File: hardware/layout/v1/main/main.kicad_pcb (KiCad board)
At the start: 4 copper layers, 32 x 52 mm, 53 parts, among them J1 12-32V + RS485, J2 Crown board, J3 Probe board, J4 PMSA003I PM, J5 Power board, Q1 AO3400A, SW1 SERVICE, U2 LM66100, U3 XIAO ESP32C6, U4 ADS1115IDGSR, U5 LSM6DS3TR-C, U6 AS3935-BQFT, U7 SP3485EN-L/TR, U8 SN74LVC2G04DBVR

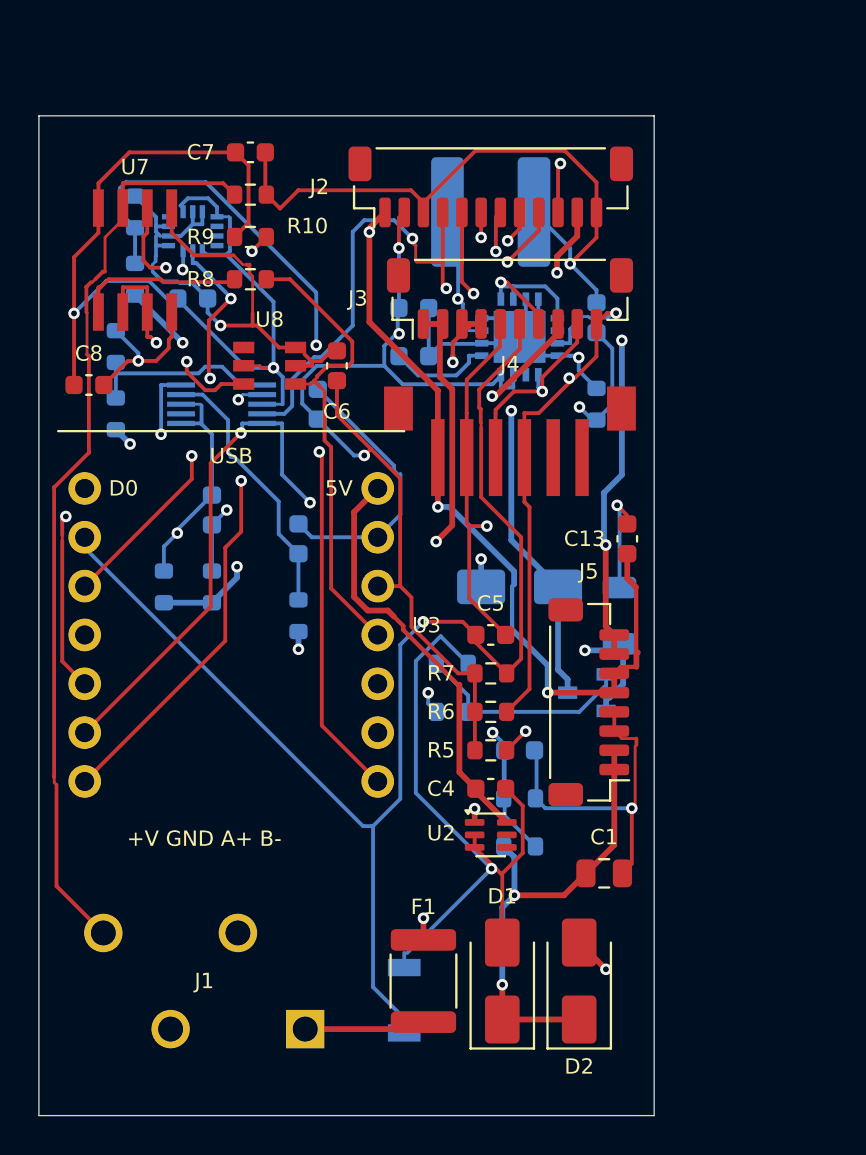
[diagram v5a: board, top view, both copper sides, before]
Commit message: Update documentation for 60V power system, STM32 crown board, 12V heaters, and expanded enclosure design
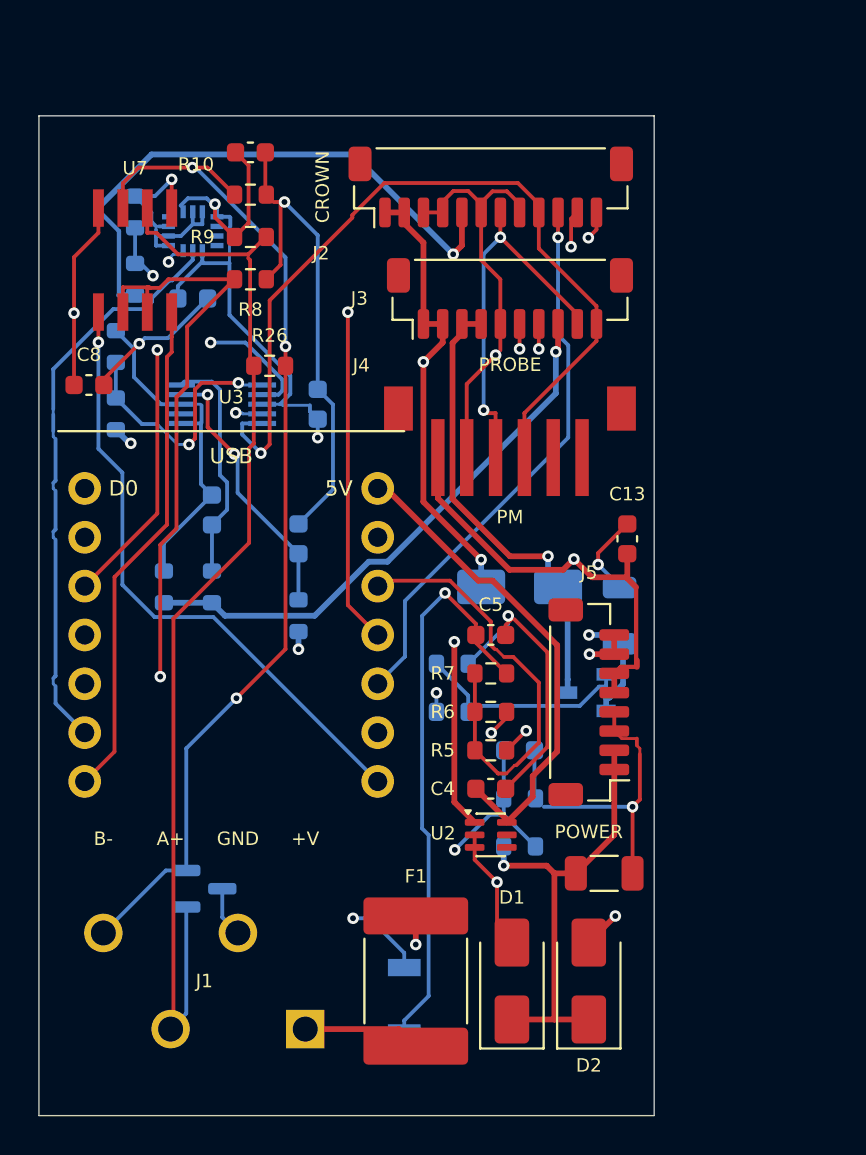
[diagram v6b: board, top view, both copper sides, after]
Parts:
- removed C10: 1u 50V, Capacitor_SMD:C_0603_1608Metric
- removed C11, C6: 100n 50V, Capacitor_SMD:C_0603_1608Metric
- removed C12: 470p C0G 50V, Capacitor_SMD:C_0603_1608Metric
- removed L2: 220uH, Inductor_SMD:L_Sunlord_SWPA6045S
- removed R11: 10k, Resistor_SMD:R_0603_1608Metric
- removed U6: AS3935-BQFT, gateway_fp:ScioSense_AS3935_QFN-16
- removed U8: SN74LVC2G04DBVR, gateway_fp:TI_SN74LVC2G04_SOT-23-6
- added D4: PSM712, Package_TO_SOT_SMD:SOT-23, B.Cu at (8.60, -11.8)
- added R26: 120R, Resistor_SMD:R_0603_1608Metric, F.Cu at (12.0, -39.0)
- C1: value 10u 50V -> 2u2 100V; footprint Capacitor_SMD:C_0805_2012Metric -> Capacitor_SMD:C_1206_3216Metric
- D1: value SMAJ33A -> SMAJ36A
- F1: footprint Fuse:Fuse_1812_4532Metric -> Fuse:Fuse_2920_7451Metric
- R10, R9: value 4k7 -> 390R
- R20: value 10k -> 30k
- R5, R6: value 4k7 -> 2k2
- R8: value 1k -> 10k
- moved D1 0.50 mm to (24.6, -7.00)
- moved D2 0.50 mm to (28.6, -7.00)
- moved F1 0.40 mm to (19.6, -7.00)
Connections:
- D3 pad 1: +5V_HEAT -> +12V_HEAT
- J2 pad 1: +5V -> +12V_HEAT
- J2 pad 10: RAIN_ADC -> CROWN_IRQ
- J2 pad 11: +5V_HEAT -> CROWN_NRST
- J2 pad 12: GND -> CROWN_BOOT0
- J2 pad 2: +3V3 -> +12V_HEAT
- J2 pad 4: I2C_SDA -> GND
- J2 pad 5: I2C_SCL -> +5V
- J2 pad 6: US_SEL_A -> GND
- J2 pad 7: US_SEL_B -> I2C_SDA
- J2 pad 8: US_TX -> GND
- J2 pad 9: US_RX -> I2C_SCL
- J3 pad 1: +5V_HEAT -> +12V_HEAT
- J3 pad 2: +5V_HEAT -> +12V_HEAT
- J5 pad 7: +5V_HEAT -> +12V_HEAT
- J5 pad 8: +5V_HEAT -> +12V_HEAT
- R20 pad 1: +5V_HEAT -> +12V_HEAT
- R8 pad 1: RS485_RO -> RS485_DE
- R8 pad 2: RS485_IO -> GND
- U3 pad 10: US_RX -> CROWN_IRQ
- U3 pad 11: RS485_IO -> CROWN_NRST
- U3 pad 3: RAIN_ADC -> CROWN_BOOT0
- U3 pad 7: US_SEL_A -> RS485_TX
- U3 pad 8: US_SEL_B -> RS485_RX
- U3 pad 9: US_TX -> RS485_DE
- U7 pad 1: RS485_RO -> RS485_RX
- U7 pad 4: GND -> RS485_TX
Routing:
- net +5V_HEAT: track 71.9 -> 0.00 mm, vias 6 -> 0
- net GND: track 183.2 -> 128.3 mm
- net +12V_HEAT: track 0.00 -> 53.0 mm, vias 0 -> 4
- net US_TX: track 44.0 -> 0.00 mm, vias 1 -> 0
- net US_RX: track 43.0 -> 0.00 mm, vias 1 -> 0
- net CROWN_BOOT0: track 0.00 -> 40.7 mm, vias 0 -> 2
- net US_SEL_A: track 38.8 -> 0.00 mm, vias 2 -> 0
- net RAIN_ADC: track 37.4 -> 0.00 mm, vias 2 -> 0
- net US_SEL_B: track 36.0 -> 0.00 mm, vias 2 -> 0
- net +5V: track 65.4 -> 98.8 mm, vias 5 -> 3
- net CROWN_NRST: track 0.00 -> 32.4 mm, vias 0 -> 2
- net RS485_RX: track 0.00 -> 32.2 mm, vias 0 -> 1
- net RS485_DE: track 11.7 -> 43.4 mm, vias 2 -> 1
- net CROWN_IRQ: track 0.00 -> 28.8 mm, vias 0 -> 1
- net RS485_TX: track 0.00 -> 26.3 mm
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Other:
- board text added: "+V"
- board text added: "A+"
- board text added: "B-"
- board text added: "GND"
- board text added: "POWER"
- board text removed: "+V GND A+ B-"

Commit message: Update documentation for column-packed breakaway panel, probe LDO rail, mast clamp dimensions, transducer adapter redesign, crown SWD/auto-flash workflow, and enclosure print plate organization
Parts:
- J5: footprint Connector_JST:JST_SH_BM08B-SRSS-TB_1x08-1MP_P1.00mm_Vertical -> Connector_JST:JST_SH_BM10B-SRSS-TB_1x10-1MP_P1.00mm_Vertical
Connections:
- J3 pad 7: +3V3 -> +3V3_PROBE
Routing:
- net +3V3: track 109.4 -> 84.0 mm
- net I2C_SCL: track 112.0 -> 89.0 mm, vias 2 -> 4
- net GND: track 128.3 -> 150.8 mm, vias 9 -> 8
- net +3V3_PROBE: track 0.00 -> 16.8 mm, vias 0 -> 2
- net +5V: track 98.8 -> 82.3 mm, vias 3 -> 5
- net RS485_B: track 54.5 -> 67.5 mm, vias 3 -> 2
- net VIN_ADC: track 48.3 -> 36.6 mm, vias 1 -> 0
- net HEAT_PWM: track 29.0 -> 21.1 mm
- net NTC_SENSE: track 72.3 -> 80.1 mm
- net MON_5V_LOGIC: track 14.0 -> 21.4 mm
- net MON_PROBE: track 12.2 -> 17.8 mm
- net HEAT_SENSE: track 28.4 -> 22.8 mm
- net +5V_XIAO: track 25.4 -> 20.4 mm
- net CROWN_BOOT0: track 40.7 -> 36.5 mm, vias 2 -> 1
- net I2C_SDA: track 92.5 -> 88.5 mm, vias 5 -> 6
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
